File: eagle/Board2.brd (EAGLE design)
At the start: 70 x 50 mm, 11 parts

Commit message: Latest mods
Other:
- board text added: "Flight Computer v 1.0 board 2"
- board text added: "chuck@whitmer.us"
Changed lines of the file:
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@@
 <wire x1="70" y1="50" x2="0" y2="50" width="0" layer="20"/>
 <wire x1="0" y1="50" x2="0" y2="0" width="0" layer="20"/>
+<text x="3.302" y="8.382" size="1.778" layer="25" font="vector" rot="R90">Flight Computer v 1.0 board 2</text>
+<text x="68.58" y="15.24" size="1.778" layer="25" font="vector" rot="R90">chuck@whitmer.us</text>
 </plain>
 <attributes>

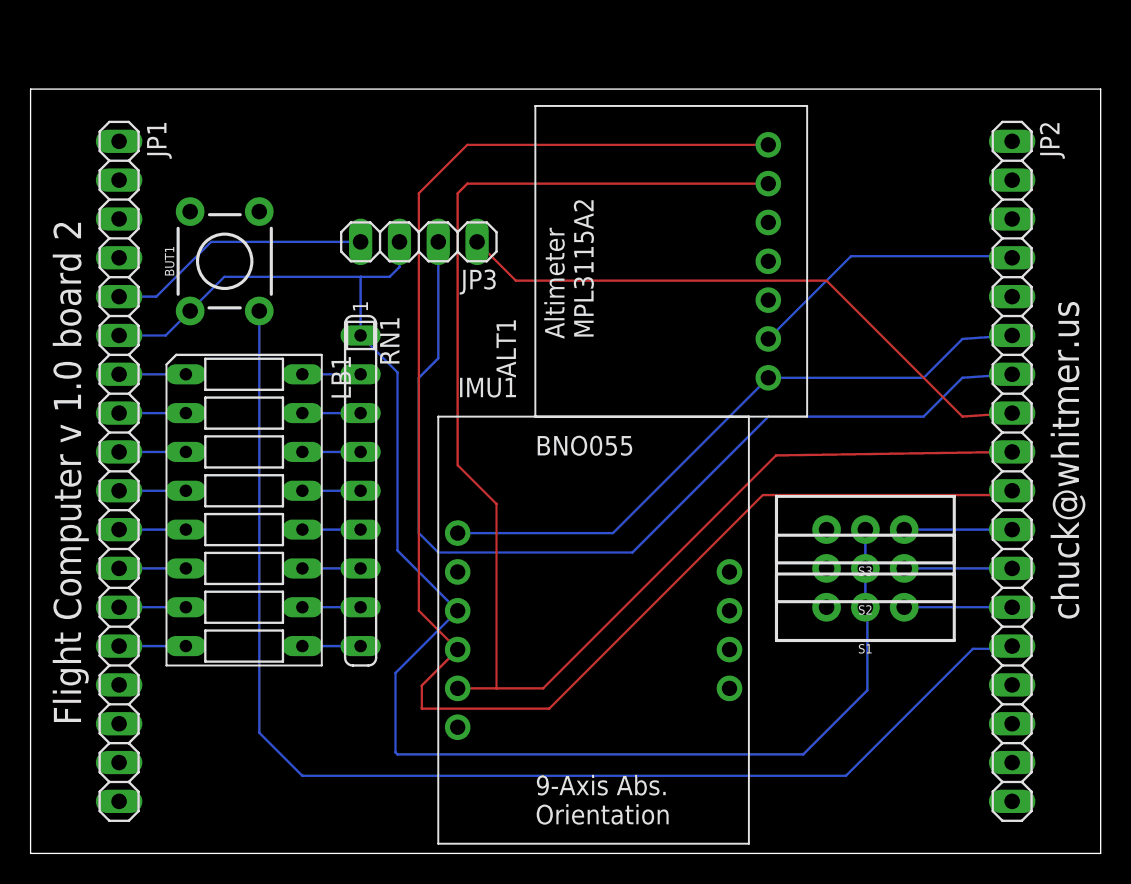
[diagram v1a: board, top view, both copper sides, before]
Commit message: Thickened lines, spread switches apart a bit
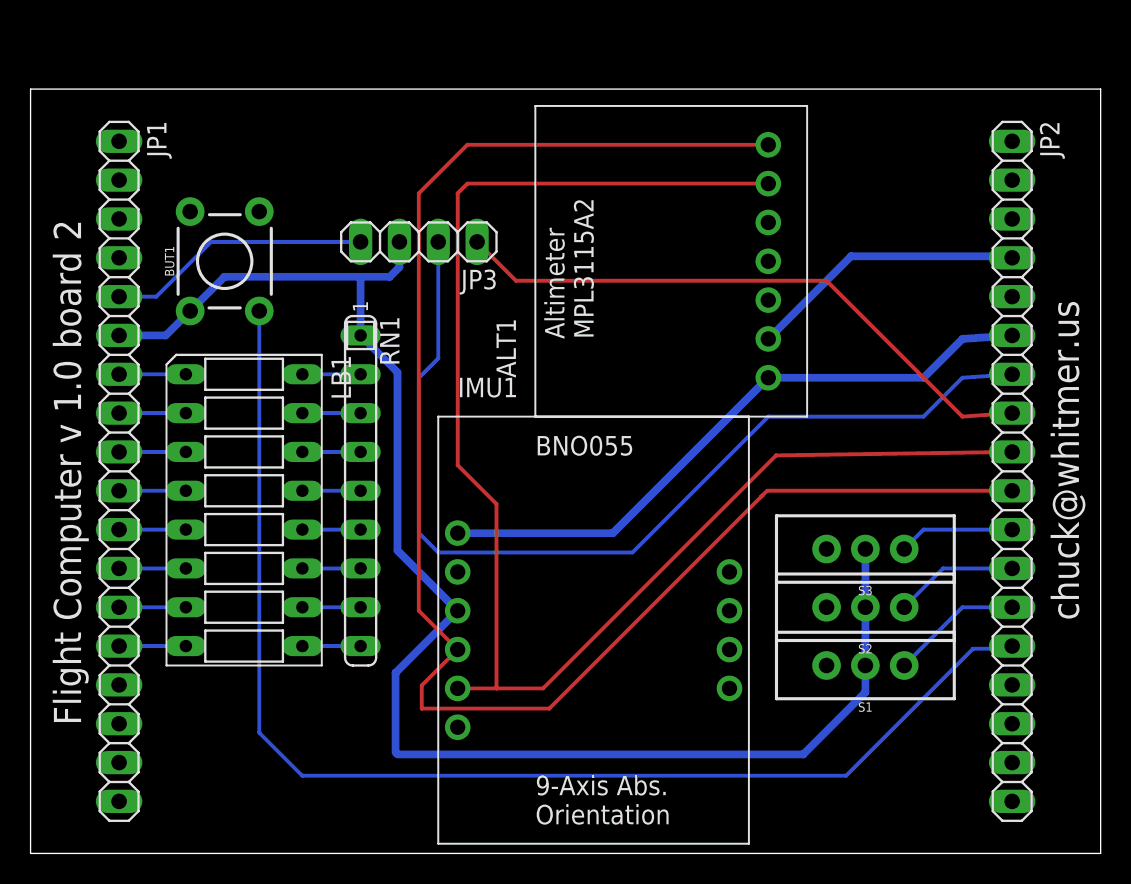
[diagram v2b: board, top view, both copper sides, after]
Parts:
- moved S1 3.81 mm to (54.6, 12.3)
- moved S2 2.54 mm to (54.6, 16.1)
- moved S3 1.27 mm to (54.6, 19.9)
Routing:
- net A1: track 7.06 -> 8.64 mm
- net GND1: track 100.5 -> 99.1 mm
- net A2: track 7.06 -> 8.11 mm
- net A3: track 7.06 -> 7.59 mm
